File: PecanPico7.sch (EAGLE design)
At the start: 161 parts, among them IC1 Si4464-B1B-FM, IC10 TC1185-1.8VCT713, IC11 TC1185-2.5VCT713, IC12 ADR380ARTZ, IC13 RF6886, IC14 ALM-GP003, IC2 Si4464-B1B-FM, IC3 BME280_BME280, IC4 UBLOX_MAX-6, IC5 STM32F429IIH6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

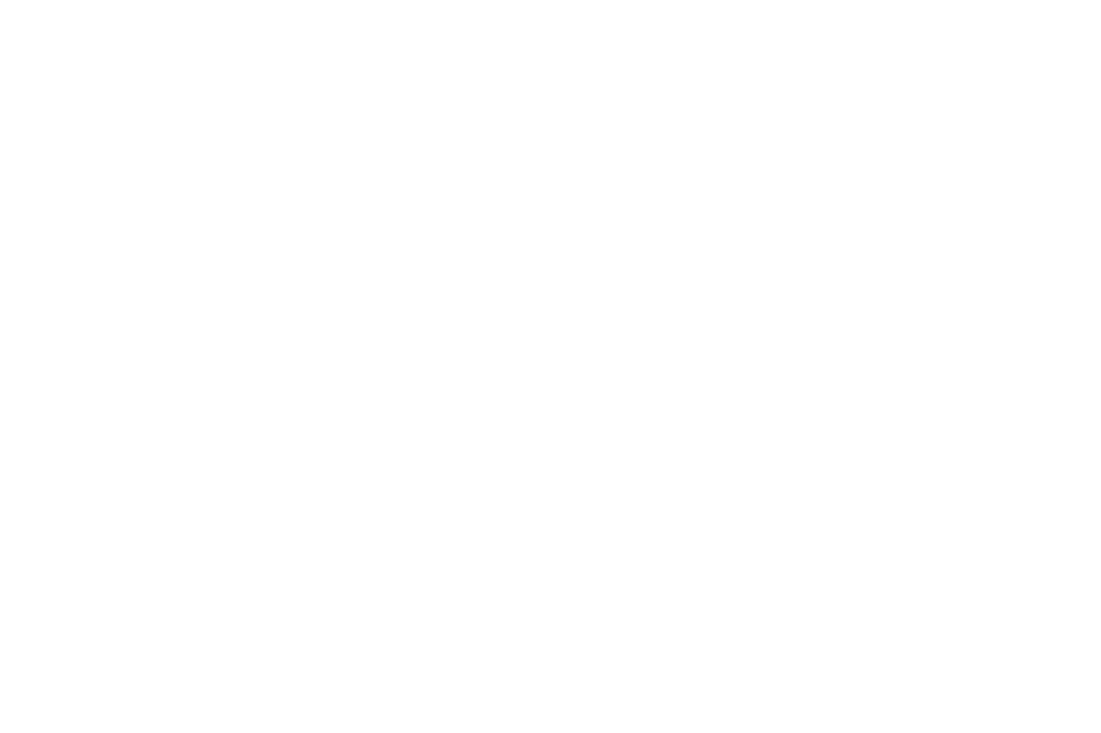
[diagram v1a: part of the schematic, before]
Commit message: Added MPU9250
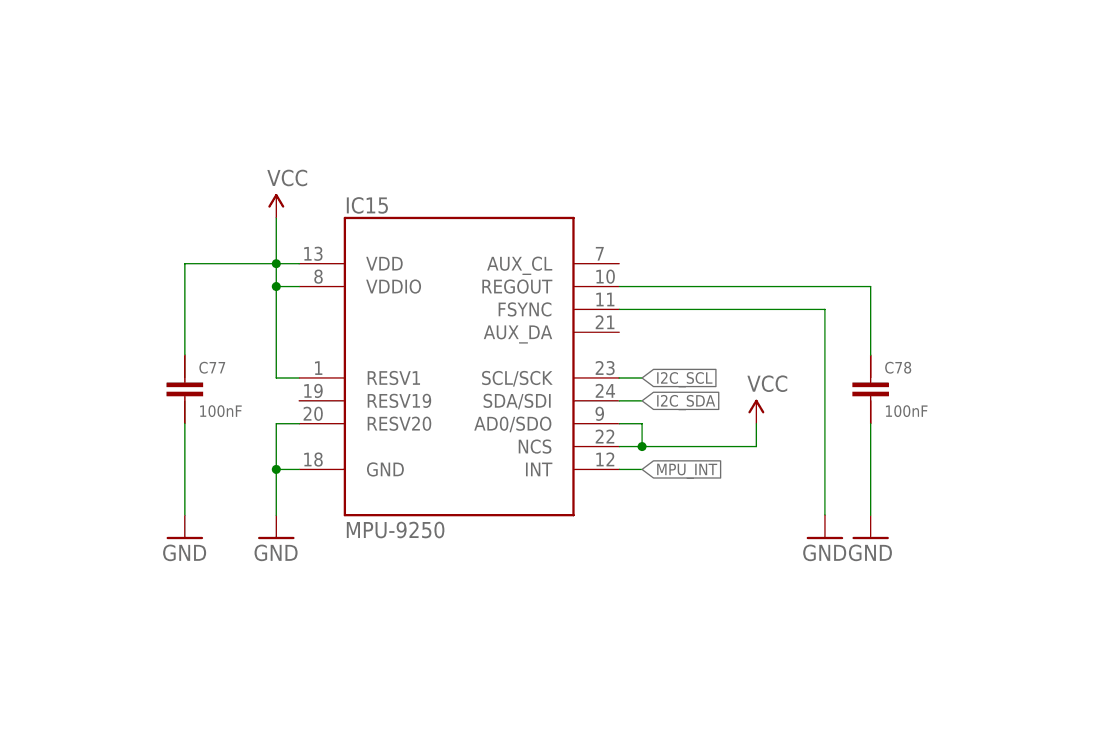
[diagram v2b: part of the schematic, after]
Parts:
- added C77, C78: 100nF, PecanPico6:CAP-0402
- added IC15: MPU-9250, SparkFun-Sensors:MPU-9250
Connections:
- new net MPU_INT: IC15.INT
- new net N$52: C78.2, IC15.REGOUT
- net GND: now also C77.1, C78.1, IC15.FSYNC, IC15.GND, IC15.RESV20
- net I2C_SCL: now also IC15.SCL/SCK
- net I2C_SDA: now also IC15.SDA/SDI
- net VCC: now also C77.2, IC15.AD0/SDO, IC15.NCS, IC15.RESV1, IC15.VDD, IC15.VDDIO
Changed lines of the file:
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@@
 <part name="C76" library="PecanPico6" deviceset="CAP-0402" device="" value=""/>
 <part name="GND98" library="PecanPico6" deviceset="GND" device=""/>
+<part name="IC15" library="SparkFun-Sensors" deviceset="MPU-9250" device=""/>
+<part name="P+39" library="PecanPico6" deviceset="3.3V" device="" value="VCC"/>
+<part name="P+40" library="PecanPico6" deviceset="3.3V" device="" value="VCC"/>
+<part name="GND99" library="PecanPico6" deviceset="GND" device=""/>
+<part name="C77" library="PecanPico6" deviceset="CAP-0402" device="" value="100nF"/>
+<part name="GND100" library="PecanPico6" deviceset="GND" device=""/>
+<part name="C78" library="PecanPico6" deviceset="CAP-0402" device="" value="100nF"/>
+<part name="GND101" library="PecanPico6" deviceset="GND" device=""/>
+<part name="GND102" library="PecanPico6" deviceset="GND" device=""/>
 </parts>
 <sheets>
@@
 <instance part="C76" gate="G$1" x="78.74" y="429.26"/>
 <instance part="GND98" gate="1" x="78.74" y="419.1"/>
+<instance part="IC15" gate="G$1" x="-38.1" y="309.88"/>
+<instance part="P+39" gate="G$1" x="-58.42" y="325.12"/>
+<instance part="P+40" gate="G$1" x="-5.08" y="302.26"/>
+<instance part="GND99" gate="1" x="-58.42" y="289.56"/>
+<instance part="C77" gate="G$1" x="-68.58" y="307.34"/>
+<instance part="GND100" gate="1" x="-68.58" y="289.56"/>
+<instance part="C78" gate="G$1" x="7.62" y="307.34"/>
+<instance part="GND101" gate="1" x="7.62" y="289.56"/>
+<instance part="GND102" gate="1" x="2.54" y="289.56"/>
 </instances>
 <busses>
@@
 <wire x1="78.74" y1="421.64" x2="78.74" y2="424.18" width="0.1524" layer="91"/>
 </segment>
+<segment>
+<pinref part="IC15" gate="G$1" pin="RESV20"/>
+<wire x1="-55.88" y1="302.26" x2="-58.42" y2="302.26" width="0.1524" layer="91"/>
+<wire x1="-58.42" y1="302.26" x2="-58.42" y2="297.18" width="0.1524" layer="91"/>
+<pinref part="IC15" gate="G$1" pin="GND"/>
+<wire x1="-58.42" y1="297.18" x2="-58.42" y2="292.1" width="0.1524" layer="91"/>
+<wire x1="-58.42" y1="297.18" x2="-55.88" y2="297.18" width="0.1524" layer="91"/>
+<junction x="-58.42" y="297.18"/>
+<pinref part="GND99" gate="1" pin="GND"/>
+</segment>
+<segment>
+<pinref part="C77" gate="G$1" pin="1"/>
+<pinref part="GND100" gate="1" pin="GND"/>
+<wire x1="-68.58" y1="292.1" x2="-68.58" y2="302.26" width="0.1524" layer="91"/>
+</segment>
+<segment>
+<pinref part="C78" gate="G$1" pin="1"/>
+<pinref part="GND101" gate="1" pin="GND"/>
+<wire x1="7.62" y1="292.1" x2="7.62" y2="302.26" width="0.1524" layer="91"/>
+</segment>
+<segment>
+<pinref part="IC15" gate="G$1" pin="FSYNC"/>
+<wire x1="-20.32" y1="314.96" x2="2.54" y2="314.96" width="0.1524" layer="91"/>
+<wire x1="2.54" y1="314.96" x2="2.54" y2="292.1" width="0.1524" layer="91"/>
+<pinref part="GND102" gate="1" pin="GND"/>
+</segment>
 </net>
 <net name="N$5" class="0">
@@
 <pinref part="P+37" gate="G$1" pin="VCC"/>
 </segment>
+<segment>
+<pinref part="IC15" gate="G$1" pin="NCS"/>
+<pinref part="P+40" gate="G$1" pin="VCC"/>
+<wire x1="-20.32" y1="299.72" x2="-17.78" y2="299.72" width="0.1524" layer="91"/>
+<wire x1="-17.78" y1="299.72" x2="-5.08" y2="299.72" width="0.1524" layer="91"/>
+<wire x1="-5.08" y1="299.72" x2="-5.08" y2="302.26" width="0.1524" layer="91"/>
+<pinref part="IC15" gate="G$1" pin="AD0/SDO"/>
+<wire x1="-20.32" y1="302.26" x2="-17.78" y2="302.26" width="0.1524" layer="91"/>
+<wire x1="-17.78" y1="302.26" x2="-17.78" y2="299.72" width="0.1524" layer="91"/>
+<junction x="-17.78" y="299.72"/>
+</segment>
+<segment>
+<pinref part="P+39" gate="G$1" pin="VCC"/>
+<pinref part="IC15" gate="G$1" pin="VDD"/>
+<wire x1="-58.42" y1="317.5" x2="-58.42" y2="320.04" width="0.1524" layer="91"/>
+<wire x1="-58.42" y1="320.04" x2="-58.42" y2="325.12" width="0.1524" layer="91"/>
+<wire x1="-55.88" y1="320.04" x2="-58.42" y2="320.04" width="0.1524" layer="91"/>
+<junction x="-58.42" y="320.04"/>
+<pinref part="IC15" gate="G$1" pin="VDDIO"/>
+<wire x1="-58.42" y1="317.5" x2="-55.88" y2="317.5" width="0.1524" layer="91"/>
+<pinref part="C77" gate="G$1" pin="2"/>
+<wire x1="-68.58" y1="309.88" x2="-68.58" y2="320.04" width="0.1524" layer="91"/>
+<wire x1="-68.58" y1="320.04" x2="-58.42" y2="320.04" width="0.1524" layer="91"/>
+<pinref part="IC15" gate="G$1" pin="RESV1"/>
+<wire x1="-58.42" y1="317.5" x2="-58.42" y2="307.34" width="0.1524" layer="91"/>
+<wire x1="-58.42" y1="307.34" x2="-55.88" y2="307.34" width="0.1524" layer="91"/>
+<junction x="-58.42" y="317.5"/>
+</segment>
 </net>
 <net name="N$14" class="0">
@@
 <pinref part="JP1" gate="G$1" pin="4"/>
 </segment>
+<segment>
+<pinref part="IC15" gate="G$1" pin="SDA/SDI"/>
+<wire x1="-20.32" y1="304.8" x2="-17.78" y2="304.8" width="0.1524" layer="91"/>
+<label x="-17.78" y="304.8" size="1.27" layer="95" xref="yes"/>
+</segment>
 </net>
 <net name="I2C_SCL" class="0">
@@
 <pinref part="JP1" gate="G$1" pin="3"/>
 </segment>
+<segment>
+<pinref part="IC15" gate="G$1" pin="SCL/SCK"/>
+<wire x1="-20.32" y1="307.34" x2="-17.78" y2="307.34" width="0.1524" layer="91"/>
+<label x="-17.78" y="307.34" size="1.27" layer="95" xref="yes"/>
+</segment>
 </net>
 <net name="GPS_RESET" class="0">
@@
 </segment>
 </net>
+<net name="MPU_INT" class="0">
+<segment>
+<pinref part="IC15" gate="G$1" pin="INT"/>
+<wire x1="-20.32" y1="297.18" x2="-17.78" y2="297.18" width="0.1524" layer="91"/>
+<label x="-17.78" y="297.18" size="1.27" layer="95" xref="yes"/>
+</segment>
+</net>
+<net name="N$52" class="0">
+<segment>
+<pinref part="IC15" gate="G$1" pin="REGOUT"/>
+<pinref part="C78" gate="G$1" pin="2"/>
+<wire x1="-20.32" y1="317.5" x2="7.62" y2="317.5" width="0.1524" layer="91"/>
+<wire x1="7.62" y1="317.5" x2="7.62" y2="309.88" width="0.1524" layer="91"/>
+</segment>
+</net>

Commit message: Connected GNDs
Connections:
- net GPS_OFF: now also IC5G$2.PE7; no longer IC5G$2.PE10
- net GPS_RESET: now also IC5G$2.PE12; no longer IC5G$2.PE15
- net MPU_INT: now also IC5G$2.PE15
- net TIMEPULSE: now also IC5G$2.PE10; no longer IC5G$2.PE12
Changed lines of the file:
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@@
 </segment>
 <segment>
-<pinref part="IC5" gate="G$2" pin="PE15"/>
-<wire x1="152.4" y1="106.68" x2="101.6" y2="106.68" width="0.1524" layer="91"/>
-<label x="101.6" y="106.68" size="1.27" layer="95" rot="R180" xref="yes"/>
+<label x="101.6" y="114.3" size="1.27" layer="95" rot="R180" xref="yes"/>
+<pinref part="IC5" gate="G$2" pin="PE12"/>
+<wire x1="152.4" y1="114.3" x2="101.6" y2="114.3" width="0.1524" layer="91"/>
 </segment>
 </net>
@@
 </segment>
 <segment>
-<pinref part="IC5" gate="G$2" pin="PE10"/>
-<wire x1="152.4" y1="119.38" x2="101.6" y2="119.38" width="0.1524" layer="91"/>
-<label x="101.6" y="119.38" size="1.27" layer="95" rot="R180" xref="yes"/>
+<label x="101.6" y="127" size="1.27" layer="95" rot="R180" xref="yes"/>
+<pinref part="IC5" gate="G$2" pin="PE7"/>
+<wire x1="152.4" y1="127" x2="101.6" y2="127" width="0.1524" layer="91"/>
 </segment>
 </net>
@@
 </segment>
 <segment>
-<pinref part="IC5" gate="G$2" pin="PE12"/>
-<wire x1="101.6" y1="114.3" x2="152.4" y2="114.3" width="0.1524" layer="91"/>
-<label x="101.6" y="114.3" size="1.27" layer="95" rot="R180" xref="yes"/>
+<wire x1="101.6" y1="119.38" x2="152.4" y2="119.38" width="0.1524" layer="91"/>
+<label x="101.6" y="119.38" size="1.27" layer="95" rot="R180" xref="yes"/>
+<pinref part="IC5" gate="G$2" pin="PE10"/>
 </segment>
 </net>
@@
 <label x="-17.78" y="297.18" size="1.27" layer="95" xref="yes"/>
 </segment>
-</net>
+<segment>
+<pinref part="IC5" gate="G$2" pin="PE15"/>
+<wire x1="152.4" y1="106.68" x2="101.6" y2="106.68" width="0.1524" layer="91"/>
+<label x="101.6" y="106.68" size="1.27" layer="95" rot="R180" xref="yes"/>
+</segment>
+</net>

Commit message: Fixed errors Fixed wrong connected DCMI pins Fixed missing I2C pull ups Fixed missing voltage dividers at ADC
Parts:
- added R37, R38: 390R, PecanPico6:RES-0402
- added R39, R40: 10k, PecanPico6:RES-0402
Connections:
- net CAM_D7: now also IC5G$1.PB6; no longer IC5G$1.PB4
- net CAM_SIOC: now also R39.1
- net CAM_SIOD: now also R40.1
- net GND: now also R37.1, R38.1
- net PWR_REF: now also R37.2
- net PWR_SENSE: now also R38.2
- net VCC: now also R39.2, R40.2; no longer IC5G$1.PC3
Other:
- moved on the sheet: C25, C51, C64, C73, C74, C75, C76, IC14, IC3, L15, L2, R26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

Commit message: Fixed errors, moved parts around Fixed GPS BIAS preamp connection Corrected GND polygons Added NRST pullup Added BYPASS_REG pullup Implemented I2C pullups for camera Checked all label connections to microcontroller Checked programming interface connections Checked STM32F4 package Fixed DCMI connection Fixed DRC errors
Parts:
- added R41, R42: 10k, PecanPico6:RES-0402
- added SJ1: (no value), PecanPico6:SJ2W
- renumbered U2 to IC16
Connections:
- removed net BYPASS_REG: IC5G$3.BYPASS_REG
- new net N$53: IC5G$3.BYPASS_REG, R41.1
- new net N$54: IC4.15_RESERVED, SJ1.3
- net GPS_BIAS: now also SJ1.2; no longer IC4.14_VCC_RF
- net NRST: now also R42.1
- net VCC: now also R41.2, R42.2, SJ1.1
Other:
- moved on the sheet: C74, C75, C76, IC14, L15, L2, R12, R35, R36

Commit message: Removed SD MOSFET, Added VSOL pad
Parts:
- removed Q3: AP2301, PecanPico6:MOSFET-PCHANNEL
- removed R23: 47k, PecanPico6:RES-0402
- added JP2: (no value), SparkFun-Connectors:M01SMD
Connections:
- removed net N$40: C70.1, C71.1, Q3.D, U1.VCC
- removed net SD_OFF: Q3.G, R23.2
- net VCC: now also C70.1, C71.1, U1.VCC; no longer Q3.S, R23.1
- net VSOLAR: now also JP2.1
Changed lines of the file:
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@@
 <part name="L11" library="sven" deviceset="IND-0402" device="0805" value=""/>
 <part name="L5" library="sven" deviceset="IND-0402" device="0805" value=""/>
-<part name="Q3" library="PecanPico6" deviceset="MOSFET-PCHANNEL" device="" value="AP2301"/>
-<part name="R23" library="PecanPico6" deviceset="RES-0402" device="" value="47k"/>
 <part name="P+35" library="PecanPico6" deviceset="3.3V" device="" value="VCC"/>
 <part name="C71" library="PecanPico6" deviceset="CAP-0402" device="" value="2.2uF"/>
@@
 <part name="SJ1" library="PecanPico6" deviceset="SJ2W" device=""/>
 <part name="P+44" library="PecanPico6" deviceset="3.3V" device="" value="VCC"/>
+<part name="JP2" library="SparkFun-Connectors" deviceset="M01" device="SMD"/>
 </parts>
 <sheets>
@@
 <instance part="L11" gate="G$1" x="538.48" y="419.1"/>
 <instance part="L5" gate="G$1" x="401.32" y="403.86"/>
-<instance part="Q3" gate="G$1" x="299.72" y="167.64" rot="MR180"/>
-<instance part="R23" gate="G$1" x="292.1" y="175.26" rot="MR0"/>
-<instance part="P+35" gate="G$1" x="299.72" y="180.34" rot="MR0"/>
+<instance part="P+35" gate="G$1" x="299.72" y="162.56" rot="MR0"/>
 <instance part="C71" gate="G$1" x="289.56" y="137.16" rot="R180"/>
 <instance part="GND21" gate="1" x="289.56" y="121.92"/>
@@
 <instance part="SJ1" gate="G$1" x="139.7" y="386.08"/>
 <instance part="P+44" gate="G$1" x="139.7" y="406.4"/>
+<instance part="JP2" gate="G$1" x="-241.3" y="421.64"/>
 </instances>
 <busses>
@@
 </segment>
 <segment>
-<pinref part="Q3" gate="G$1" pin="S"/>
-<wire x1="299.72" y1="172.72" x2="299.72" y2="175.26" width="0.1524" layer="91"/>
-<pinref part="R23" gate="G$1" pin="1"/>
-<wire x1="299.72" y1="175.26" x2="297.18" y2="175.26" width="0.1524" layer="91"/>
-<wire x1="299.72" y1="175.26" x2="299.72" y2="180.34" width="0.1524" layer="91"/>
-<junction x="299.72" y="175.26"/>
 <pinref part="P+35" gate="G$1" pin="VCC"/>
+<pinref part="U1" gate="G$1" pin="VCC"/>
+<wire x1="299.72" y1="152.4" x2="320.04" y2="152.4" width="0.1524" layer="91"/>
+<pinref part="C70" gate="G$1" pin="1"/>
+<wire x1="299.72" y1="142.24" x2="299.72" y2="152.4" width="0.1524" layer="91"/>
+<junction x="299.72" y="152.4"/>
+<pinref part="C71" gate="G$1" pin="1"/>
+<wire x1="289.56" y1="142.24" x2="289.56" y2="152.4" width="0.1524" layer="91"/>
+<wire x1="289.56" y1="152.4" x2="299.72" y2="152.4" width="0.1524" layer="91"/>
+<wire x1="299.72" y1="162.56" x2="299.72" y2="152.4" width="0.1524" layer="91"/>
 </segment>
 <segment>
@@
 <junction x="-205.74" y="421.64"/>
 <wire x1="-215.9" y1="421.64" x2="-205.74" y2="421.64" width="0.1524" layer="91"/>
-<wire x1="-228.6" y1="421.64" x2="-233.68" y2="421.64" width="0.1524" layer="91"/>
 <junction x="-228.6" y="421.64"/>
 <wire x1="-228.6" y1="421.64" x2="-228.6" y2="416.56" width="0.1524" layer="91"/>
 <pinref part="C46" gate="G$1" pin="2"/>
-<label x="-233.68" y="421.64" size="1.27" layer="95" rot="R180" xref="yes"/>
 <pinref part="L13" gate="G$1" pin="1"/>
 <wire x1="-215.9" y1="419.1" x2="-215.9" y2="421.64" width="0.1524" layer="91"/>
 <junction x="-215.9" y="421.64"/>
+<pinref part="JP2" gate="G$1" pin="1"/>
+<wire x1="-233.68" y1="421.64" x2="-228.6" y2="421.64" width="0.1524" layer="91"/>
+<wire x1="-167.64" y1="421.64" x2="-144.78" y2="421.64" width="0.1524" layer="91"/>
+<junction x="-167.64" y="421.64"/>
+<label x="-144.78" y="421.64" size="1.27" layer="95" xref="yes"/>
 </segment>
 <segment>
@@
 </segment>
 </net>
-<net name="N$40" class="0">
-<segment>
-<pinref part="U1" gate="G$1" pin="VCC"/>
-<wire x1="299.72" y1="162.56" x2="299.72" y2="152.4" width="0.1524" layer="91"/>
-<wire x1="299.72" y1="152.4" x2="320.04" y2="152.4" width="0.1524" layer="91"/>
-<pinref part="C70" gate="G$1" pin="1"/>
-<wire x1="299.72" y1="142.24" x2="299.72" y2="152.4" width="0.1524" layer="91"/>
-<junction x="299.72" y="152.4"/>
-<pinref part="Q3" gate="G$1" pin="D"/>
-<pinref part="C71" gate="G$1" pin="1"/>
-<wire x1="289.56" y1="142.24" x2="289.56" y2="152.4" width="0.1524" layer="91"/>
-<wire x1="289.56" y1="152.4" x2="299.72" y2="152.4" width="0.1524" layer="91"/>
-</segment>
-</net>
-<net name="SD_OFF" class="0">
-<segment>
-<pinref part="R23" gate="G$1" pin="2"/>
-<wire x1="287.02" y1="175.26" x2="284.48" y2="175.26" width="0.1524" layer="91"/>
-<wire x1="284.48" y1="175.26" x2="284.48" y2="167.64" width="0.1524" layer="91"/>
-<pinref part="Q3" gate="G$1" pin="G"/>
-<wire x1="284.48" y1="167.64" x2="292.1" y2="167.64" width="0.1524" layer="91"/>
-<wire x1="284.48" y1="167.64" x2="281.94" y2="167.64" width="0.1524" layer="91"/>
-<junction x="284.48" y="167.64"/>
-<label x="281.94" y="167.64" size="1.27" layer="95" rot="MR0" xref="yes"/>
-</segment>
-</net>
